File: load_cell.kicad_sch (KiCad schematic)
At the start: 10 parts, among them Q2 S8550, U7 HX711

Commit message: Remove duplicated power flag.
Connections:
- net +3.3V renamed +3V3
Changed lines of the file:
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@@
+	)
+	(symbol
+		(lib_id "power:+3V3")
+		(at 154.94 69.85 0)
+		(unit 1)
+		(body_style 1)
+		(exclude_from_sim no)
+		(in_bom yes)
+		(on_board yes)
+		(in_pos_files yes)
+		(dnp no)
+		(fields_autoplaced yes)
+		(property "Reference" "#PWR045"
+			(at 154.94 73.66 0)
+			(hide yes)
+			(show_name no)
+			(do_not_autoplace no)
+			(effects
+				(font
+					(size 1.27 1.27)
+				)
+			)
+		)
+		(property "Value" "+3V3"
+			(at 154.94 64.77 0)
+			(show_name no)
+			(do_not_autoplace no)
+			(effects
+				(font
+					(size 1.27 1.27)
+				)
+			)
+		)
+		(property "Footprint" ""
+			(at 154.94 69.85 0)
+			(hide yes)
+			(show_name no)
+			(do_not_autoplace no)
+			(effects
+				(font
+					(size 1.27 1.27)
+				)
+			)
+		)
+		(property "Datasheet" ""
+			(at 154.94 69.85 0)
+			(hide yes)
+			(show_name no)
+			(do_not_autoplace no)
+			(effects
+				(font
+					(size 1.27 1.27)
+				)
+			)
+		)
+		(property "Description" "Power symbol creates a global label with name \"+3V3\""
+			(at 154.94 69.85 0)
+			(hide yes)
+			(show_name no)
+			(do_not_autoplace no)
+			(effects
+				(font
+					(size 1.27 1.27)
+				)
+			)
+		)
+		(pin "1"
+		)
+		(instances
+			(project "CC3501-project-hardware"
+				(path "/4a2d49bb-8ba4-4c60-a8f0-05b8d2544445/0c27bcac-fbf5-401f-bcb4-99ca27aa5914"
+					(reference "#PWR045")
+					(unit 1)
+				)
+			)
+		)
 	)
 	(symbol
@@
 					(unit 1)
 				)
-			)
-		)
-	)
-	(symbol
-		(lib_id "power:+3.3V")
-		(at 154.94 69.85 270)
-		(unit 1)
-		(body_style 1)
-		(exclude_from_sim no)
-		(in_bom yes)
-		(on_board yes)
-		(in_pos_files yes)
-		(dnp no)
-		(fields_autoplaced yes)
-		(property "Reference" "#PWR045"
-			(at 151.13 69.85 0)
-			(hide yes)
-			(show_name no)
-			(do_not_autoplace no)
-			(effects
-				(font
-					(size 1.27 1.27)
-				)
-			)
-		)
-		(property "Value" "+3.3V"
-			(at 158.75 69.8499 90)
-			(show_name no)
-			(do_not_autoplace no)
-			(effects
-				(font
-					(size 1.27 1.27)
-				)
-				(justify left)
-			)
-		)
-		(property "Footprint" ""
-			(at 154.94 69.85 0)
-			(hide yes)
-			(show_name no)
-			(do_not_autoplace no)
-			(effects
-				(font
-					(size 1.27 1.27)
-				)
-			)
-		)
-		(property "Datasheet" ""
-			(at 154.94 69.85 0)
-			(hide yes)
-			(show_name no)
-			(do_not_autoplace no)
-			(effects
-				(font
-					(size 1.27 1.27)
-				)
-			)
-		)
-		(property "Description" "Power symbol creates a global label with name \"+3.3V\""
-			(at 154.94 69.85 0)
-			(hide yes)
-			(show_name no)
-			(do_not_autoplace no)
-			(effects
-				(font
-					(size 1.27 1.27)
-				)
-			)
-		)
-		(pin "1"
-		)
-		(instances
-			(project "CC3501-project-hardware"
-				(path "/4a2d49bb-8ba4-4c60-a8f0-05b8d2544445/0c27bcac-fbf5-401f-bcb4-99ca27aa5914"
-					(reference "#PWR045")
-					(unit 1)
-				)

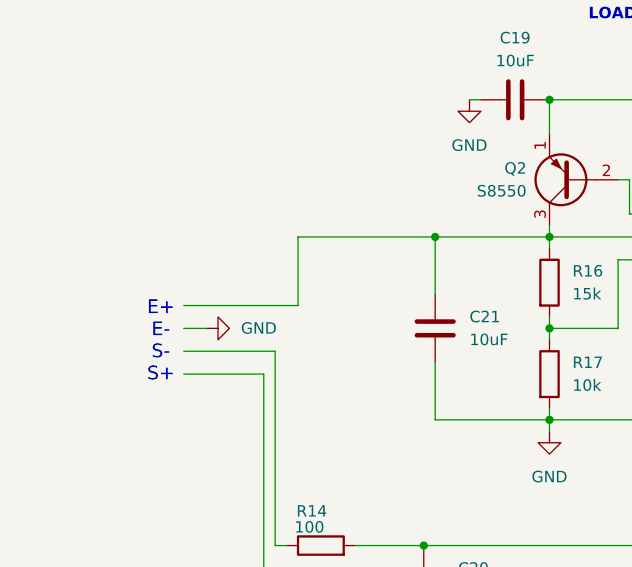
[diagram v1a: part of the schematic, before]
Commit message: Rewire TFT display to power with 5V and allowing backlight switching via FET.
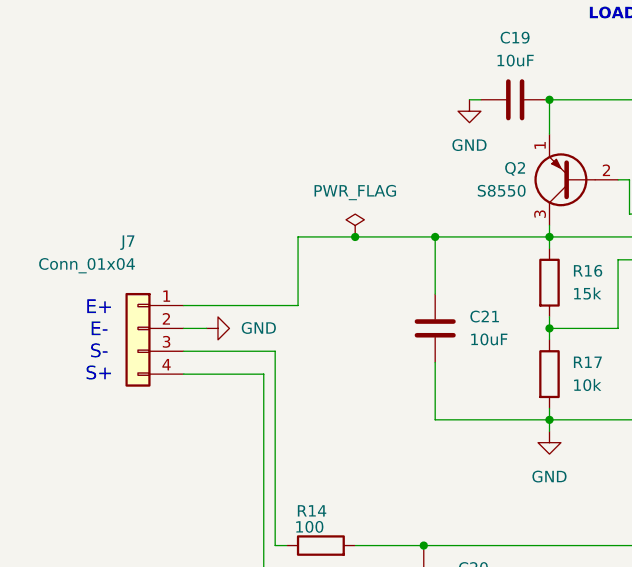
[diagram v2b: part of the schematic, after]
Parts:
- added J7: Conn_01x04, symbol Connector_Generic:Conn_01x04
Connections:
- net GND: now also J7.2 (Pin_2)
- net at R15.2: now also J7.4 (Pin_4)
- net at C21.1, Q2.3 (C), R16.1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: now also J7.1 (Pin_1)
- net at R14.1: now also J7.3 (Pin_3)
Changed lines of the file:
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@@
 	(text "E+\nE-\nS-\nS+\n"
 		(exclude_from_sim no)
-		(at 59.69 96.774 0)
+		(at 52.832 96.774 0)
 		(effects
 			(font
@@
 		(color 0 0 0 0)
 	)
+	(junction
+		(at 81.28 85.09)
+		(diameter 0)
+		(color 0 0 0 0)
+	)
 	(no_connect
 		(at 167.64 95.25)
@@
 	(wire
 		(pts
+			(xy 81.28 85.09) (xy 90.17 85.09)
+		)
+		(stroke
+			(width 0)
+			(type default)
+		)
+	)
+	(wire
+		(pts
 			(xy 138.43 115.57) (xy 138.43 116.84)
 		)
@@
 	(wire
 		(pts
-			(xy 74.93 85.09) (xy 90.17 85.09)
+			(xy 74.93 85.09) (xy 81.28 85.09)
 		)
 		(stroke
@@
 	)
 	(symbol
+		(lib_id "power:PWR_FLAG")
+		(at 81.28 85.09 0)
+		(unit 1)
+		(body_style 1)
+		(exclude_from_sim no)
+		(in_bom yes)
+		(on_board yes)
+		(in_pos_files yes)
+		(dnp no)
+		(fields_autoplaced yes)
+		(property "Reference" "#FLG06"
+			(at 81.28 83.185 0)
+			(hide yes)
+			(show_name no)
+			(do_not_autoplace no)
+			(effects
+				(font
+					(size 1.27 1.27)
+				)
+			)
+		)
+		(property "Value" "PWR_FLAG"
+			(at 81.28 80.01 0)
+			(show_name no)
+			(do_not_autoplace no)
+			(effects
+				(font
+					(size 1.27 1.27)
+				)
+			)
+		)
+		(property "Footprint" ""
+			(at 81.28 85.09 0)
+			(hide yes)
+			(show_name no)
+			(do_not_autoplace no)
+			(effects
+				(font
+					(size 1.27 1.27)
+				)
+			)
+		)
+		(property "Datasheet" ""
+			(at 81.28 85.09 0)
+			(hide yes)
+			(show_name no)
+			(do_not_autoplace no)
+			(effects
+				(font
+					(size 1.27 1.27)
+				)
+			)
+		)
+		(property "Description" "Special symbol for telling ERC where power comes from"
+			(at 81.28 85.09 0)
+			(hide yes)
+			(show_name no)
+			(do_not_autoplace no)
+			(effects
+				(font
+					(size 1.27 1.27)
+				)
+			)
+		)
+		(pin "1"
+		)
+		(instances
+			(project "CC3501-project-hardware"
+				(path "/4a2d49bb-8ba4-4c60-a8f0-05b8d2544445/0c27bcac-fbf5-401f-bcb4-99ca27aa5914"
+					(reference "#FLG06")
+					(unit 1)
+				)
+			)
+		)
+	)
+	(symbol
 		(lib_id "power:GND")
 		(at 102.87 106.68 0)
@@
 					(unit 1)
 				)
+			)
+		)
+	)
+	(symbol
+		(lib_id "Connector_Generic:Conn_01x04")
+		(at 57.15 95.25 0)
+		(mirror y)
+		(unit 1)
+		(body_style 1)
+		(exclude_from_sim no)
+		(in_bom yes)
+		(on_board yes)
+		(in_pos_files yes)
+		(dnp no)
+		(property "Reference" "J7"
+			(at 56.896 85.598 0)
+			(show_name no)
+			(do_not_autoplace no)
+			(effects
+				(font
+					(size 1.27 1.27)
+				)
+				(justify left)
+			)
+		)
+		(property "Value" "Conn_01x04"
+			(at 56.896 88.138 0)
+			(show_name no)
+			(do_not_autoplace no)
+			(effects
+				(font
+					(size 1.27 1.27)
+				)
+				(justify left)
+			)
+		)
+		(property "Footprint" ""
+			(at 57.15 95.25 0)
+			(hide yes)
+			(show_name no)
+			(do_not_autoplace no)
+			(effects
+				(font
+					(size 1.27 1.27)
+				)
+			)
+		)
+		(property "Datasheet" ""
+			(at 57.15 95.25 0)
+			(hide yes)
+			(show_name no)
+			(do_not_autoplace no)
+			(effects
+				(font
+					(size 1.27 1.27)
+				)
+			)
+		)
+		(property "Description" "Generic connector, single row, 01x04, script generated (kicad-library-utils/schlib/autogen/connector/)"
+			(at 57.15 95.25 0)
+			(hide yes)
+			(show_name no)
+			(do_not_autoplace no)
+			(effects
+				(font
+					(size 1.27 1.27)
+				)
+			)
+		)
+		(pin "2"
+		)
+		(pin "1"
+		)
+		(pin "4"
+		)
+		(pin "3"
+		)
+		(instances
+			(project "CC3501-project-hardware"
+				(path "/4a2d49bb-8ba4-4c60-a8f0-05b8d2544445/0c27bcac-fbf5-401f-bcb4-99ca27aa5914"
+					(reference "J7")
+					(unit 1)
+				)

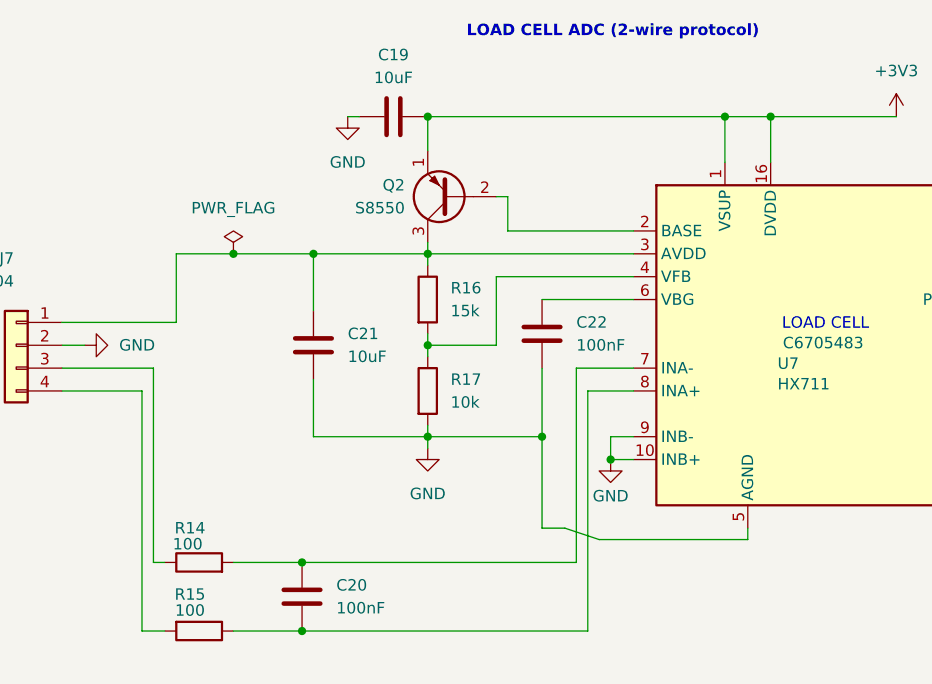
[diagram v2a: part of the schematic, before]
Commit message: edit HX711 config
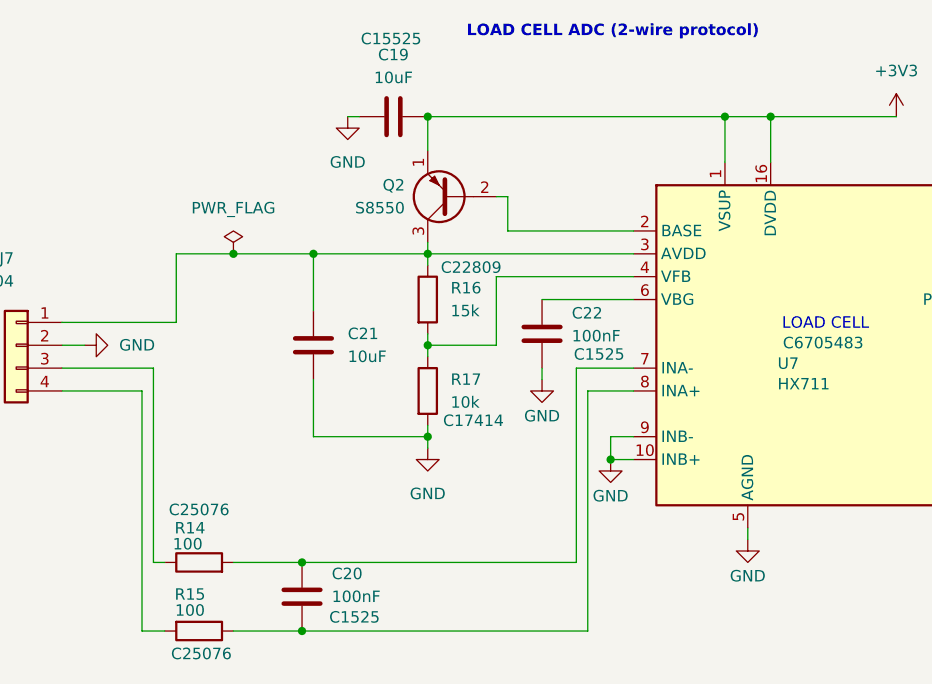
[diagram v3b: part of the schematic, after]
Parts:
- J7: footprint (none) -> Connector_PinHeader_2.54mm:PinHeader_1x04_P2.54mm_Vertical
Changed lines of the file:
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@@
 	)
 	(junction
-		(at 115.57 105.41)
-		(diameter 0)
-		(color 0 0 0 0)
-	)
-	(junction
 		(at 102.87 69.85)
 		(diameter 0)
@@
 	(wire
 		(pts
-			(xy 121.92 116.84) (xy 138.43 116.84)
-		)
-		(stroke
-			(width 0)
-			(type default)
-		)
-	)
-	(wire
-		(pts
 			(xy 72.39 119.38) (xy 73.66 119.38)
 		)
@@
 	(wire
 		(pts
-			(xy 115.57 97.79) (xy 115.57 105.41)
-		)
-		(stroke
-			(width 0)
-			(type default)
-		)
-	)
-	(wire
-		(pts
 			(xy 102.87 85.09) (xy 125.73 85.09)
 		)
@@
 	(wire
 		(pts
-			(xy 115.57 115.57) (xy 118.11 115.57)
-		)
-		(stroke
-			(width 0)
-			(type default)
-		)
-	)
-	(wire
-		(pts
 			(xy 140.97 69.85) (xy 140.97 74.93)
 		)
@@
 	(wire
 		(pts
-			(xy 118.11 115.57) (xy 121.92 116.84)
-		)
-		(stroke
-			(width 0)
-			(type default)
-		)
-	)
-	(wire
-		(pts
 			(xy 110.49 78.74) (xy 111.76 78.74)
 		)
@@
 	(wire
 		(pts
+			(xy 115.57 97.79) (xy 115.57 99.06)
+		)
+		(stroke
+			(width 0)
+			(type default)
+		)
+	)
+	(wire
+		(pts
 			(xy 102.87 104.14) (xy 102.87 105.41)
 		)
@@
 	(wire
 		(pts
-			(xy 102.87 105.41) (xy 115.57 105.41)
-		)
-		(stroke
-			(width 0)
-			(type default)
-		)
-	)
-	(wire
-		(pts
 			(xy 102.87 105.41) (xy 90.17 105.41)
 		)
@@
 	(wire
 		(pts
-			(xy 115.57 105.41) (xy 115.57 115.57)
-		)
-		(stroke
-			(width 0)
-			(type default)
-		)
-	)
-	(wire
-		(pts
 			(xy 120.65 100.33) (xy 120.65 127)
 		)
@@
 	(symbol
 		(lib_id "power:GND")
+		(at 115.57 99.06 0)
+		(unit 1)
+		(body_style 1)
+		(exclude_from_sim no)
+		(in_bom yes)
+		(on_board yes)
+		(in_pos_files yes)
+		(dnp no)
+		(property "Reference" "#PWR082"
+			(at 115.57 105.41 0)
+			(hide yes)
+			(show_name no)
+			(do_not_autoplace no)
+			(effects
+				(font
+					(size 1.27 1.27)
+				)
+			)
+		)
+		(property "Value" "GND"
+			(at 115.57 103.124 0)
+			(show_name no)
+			(do_not_autoplace no)
+			(effects
+				(font
+					(size 1.27 1.27)
+				)
+			)
+		)
+		(property "Footprint" ""
+			(at 115.57 99.06 0)
+			(hide yes)
+			(show_name no)
+			(do_not_autoplace no)
+			(effects
+				(font
+					(size 1.27 1.27)
+				)
+			)
+		)
+		(property "Datasheet" ""
+			(at 115.57 99.06 0)
+			(hide yes)
+			(show_name no)
+			(do_not_autoplace no)
+			(effects
+				(font
+					(size 1.27 1.27)
+				)
+			)
+		)
+		(property "Description" "Power symbol creates a global label with name \"GND\" , ground"
+			(at 115.57 99.06 0)
+			(hide yes)
+			(show_name no)
+			(do_not_autoplace no)
+			(effects
+				(font
+					(size 1.27 1.27)
+				)
+			)
+		)
+		(pin "1"
+		)
+		(instances
+			(project "CC3501-project-hardware"
+				(path "/4a2d49bb-8ba4-4c60-a8f0-05b8d2544445/0c27bcac-fbf5-401f-bcb4-99ca27aa5914"
+					(reference "#PWR082")
+					(unit 1)
+				)
+			)
+		)
+	)
+	(symbol
+		(lib_id "power:GND")
 		(at 102.87 106.68 0)
 		(unit 1)
@@
 		)
 		(property "LCSC PN" "C25076"
-			(at 77.47 127 90)
-			(hide yes)
+			(at 77.724 129.54 90)
 			(show_name no)
 			(do_not_autoplace no)
@@
 		)
 		(property "LCSC PN" "C15525"
-			(at 99.06 69.85 90)
-			(hide yes)
+			(at 98.806 61.214 90)
 			(show_name no)
 			(do_not_autoplace no)
@@
 		(in_pos_files yes)
 		(dnp no)
-		(fields_autoplaced yes)
 		(property "Reference" "R17"
 			(at 105.41 99.0599 0)
@@
 		)
 		(property "LCSC PN" "C17414"
-			(at 102.87 100.33 0)
-			(hide yes)
+			(at 107.95 103.632 0)
 			(show_name no)
 			(do_not_autoplace no)
@@
 		(in_pos_files yes)
 		(dnp no)
-		(fields_autoplaced yes)
 		(property "Reference" "R16"
 			(at 105.41 88.8999 0)
@@
 		)
 		(property "LCSC PN" "C22809"
-			(at 102.87 90.17 0)
-			(hide yes)
+			(at 107.696 86.614 0)
 			(show_name no)
 			(do_not_autoplace no)
@@
 		)
 		(property "LCSC PN" "C25076"
-			(at 77.47 119.38 90)
-			(hide yes)
+			(at 77.47 113.538 90)
 			(show_name no)
 			(do_not_autoplace no)
@@
 		(in_pos_files yes)
 		(dnp no)
-		(fields_autoplaced yes)
 		(property "Reference" "C22"
-			(at 119.38 92.7099 0)
+			(at 118.872 91.694 0)
 			(show_name no)
 			(do_not_autoplace no)
@@
 		)
 		(property "Value" "100nF"
-			(at 119.38 95.2499 0)
+			(at 118.872 94.234 0)
 			(show_name no)
 			(do_not_autoplace no)
@@
 		)
 		(property "LCSC PN" "C1525"
-			(at 115.57 93.98 0)
-			(hide yes)
+			(at 121.92 96.2661 0)
 			(show_name no)
 			(do_not_autoplace no)
@@
 		(in_pos_files yes)
 		(dnp no)
-		(fields_autoplaced yes)
 		(property "Reference" "C20"
-			(at 92.71 121.9199 0)
+			(at 92.202 120.65 0)
 			(show_name no)
 			(do_not_autoplace no)
@@
 		)
 		(property "Value" "100nF"
-			(at 92.71 124.4599 0)
+			(at 92.202 123.19 0)
 			(show_name no)
 			(do_not_autoplace no)
@@
 		)
 		(property "LCSC PN" "C1525"
-			(at 88.9 123.19 0)
-			(hide yes)
+			(at 94.742 125.476 0)
 			(show_name no)
 			(do_not_autoplace no)
@@
 			)
 		)
-		(property "Footprint" ""
+		(property "Footprint" "Connector_PinHeader_2.54mm:PinHeader_1x04_P2.54mm_Vertical"
 			(at 57.15 95.25 0)
 			(hide yes)
@@
 					(unit 1)
 				)
+			)
+		)
+	)
+	(symbol
+		(lib_id "power:GND")
+		(at 138.43 116.84 0)
+		(unit 1)
+		(body_style 1)
+		(exclude_from_sim no)
+		(in_bom yes)
+		(on_board yes)
+		(in_pos_files yes)
+		(dnp no)
+		(property "Reference" "#PWR043"
+			(at 138.43 123.19 0)
+			(hide yes)
+			(show_name no)
+			(do_not_autoplace no)
+			(effects
+				(font
+					(size 1.27 1.27)
+				)
+			)
+		)
+		(property "Value" "GND"
+			(at 138.43 120.904 0)
+			(show_name no)
+			(do_not_autoplace no)
+			(effects
+				(font
+					(size 1.27 1.27)
+				)
+			)
+		)
+		(property "Footprint" ""
+			(at 138.43 116.84 0)
+			(hide yes)
+			(show_name no)
+			(do_not_autoplace no)
+			(effects
+				(font
+					(size 1.27 1.27)
+				)
+			)
+		)
+		(property "Datasheet" ""
+			(at 138.43 116.84 0)
+			(hide yes)
+			(show_name no)
+			(do_not_autoplace no)
+			(effects
+				(font
+					(size 1.27 1.27)
+				)
+			)
+		)
+		(property "Description" "Power symbol creates a global label with name \"GND\" , ground"
+			(at 138.43 116.84 0)
+			(hide yes)
+			(show_name no)
+			(do_not_autoplace no)
+			(effects
+				(font
+					(size 1.27 1.27)
+				)
+			)
+		)
+		(pin "1"
+		)
+		(instances
+			(project "CC3501-project-hardware"
+				(path "/4a2d49bb-8ba4-4c60-a8f0-05b8d2544445/0c27bcac-fbf5-401f-bcb4-99ca27aa5914"
+					(reference "#PWR043")
+					(unit 1)
+				)

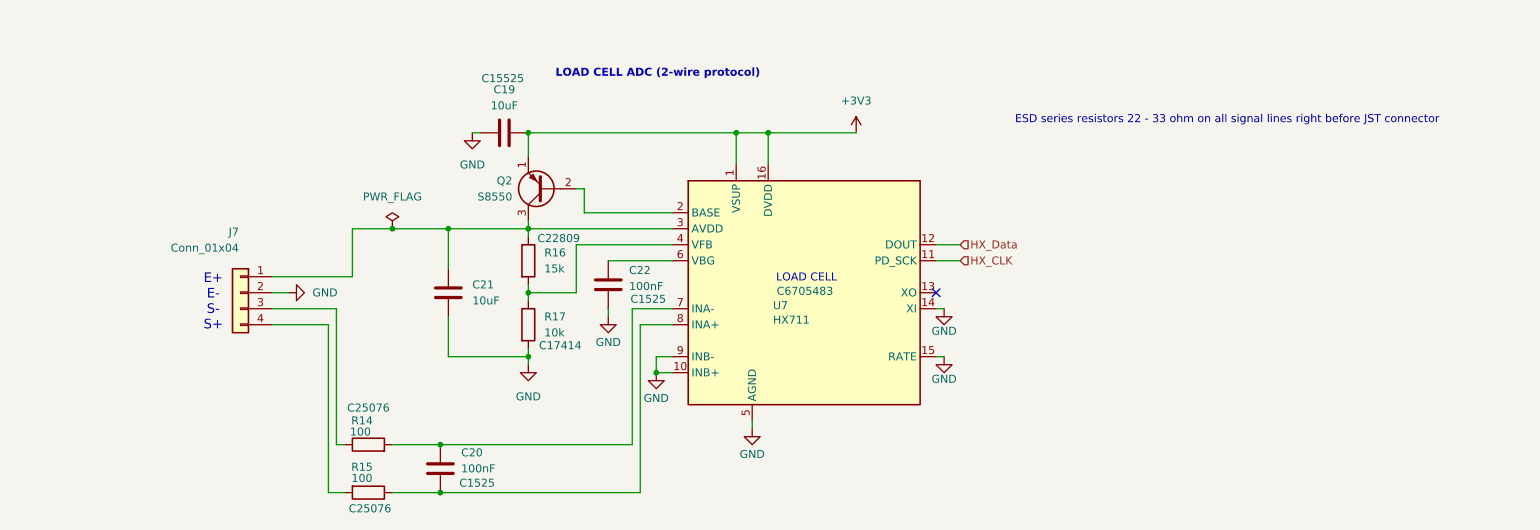
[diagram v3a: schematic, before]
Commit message: edit HX711 configuration to match datasheet and sparkfun example as well as add JLC part numbers and display them on schematic
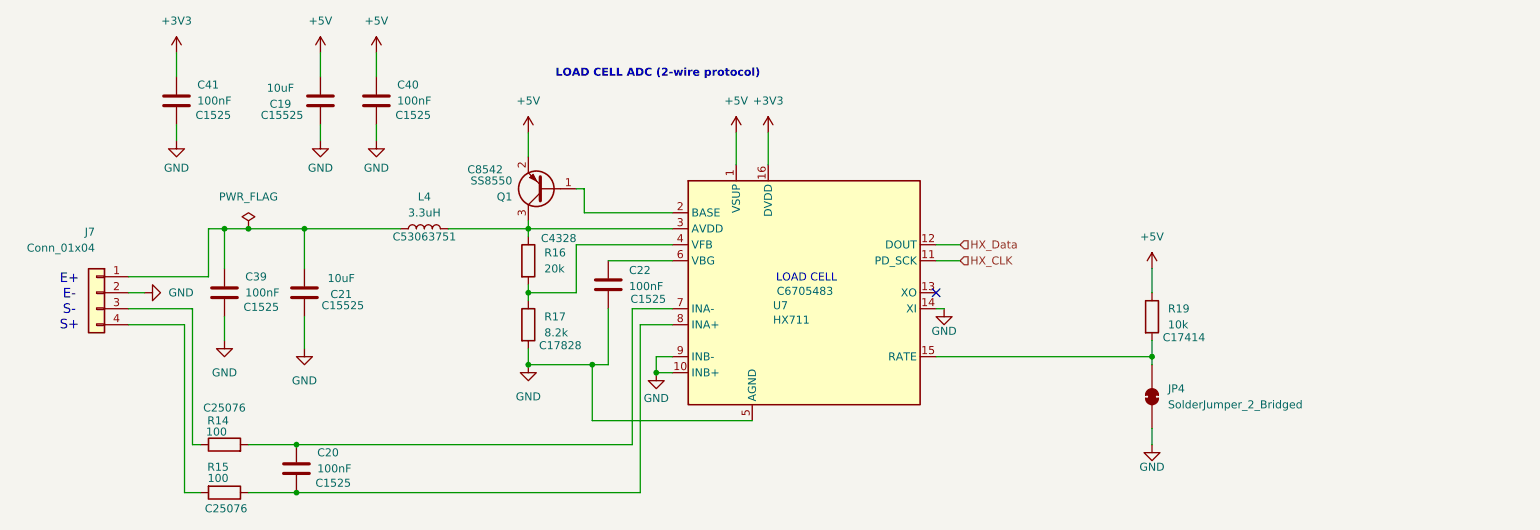
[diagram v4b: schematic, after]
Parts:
- removed Q2: S8550, Package_TO_SOT_THT:TO-92_Inline, symbol Transistor_BJT:S8550
- added C39, C40, C41: 100nF, Capacitor_SMD:C_0402_1005Metric, symbol Device:C
- added JP4: SolderJumper_2_Bridged, Jumper:SolderJumper-2_P1.3mm_Bridged2Bar_RoundedPad1.0x1.5mm, symbol Jumper:SolderJumper_2_Bridged
- added L4: 3.3uH, Inductor_SMD:L_0805_2012Metric, symbol Device:L
- added Q1: SS8550, Package_TO_SOT_SMD:SOT-23, symbol Transistor_BJT:SS8550
- added R19: 10k, Resistor_SMD:R_0805_2012Metric, symbol Device:R
- R16: value 15k -> 20k; footprint Resistor_SMD:R_0603_1608Metric -> Resistor_SMD:R_0805_2012Metric; LCSC PN C22809 -> C4328
- R17: value 10k -> 8.2k; LCSC PN C17414 -> C17828
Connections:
- net +3V3: now also C41.1; no longer C19.2, U7.1 (VSUP)
- net GND: now also C21.1, C39.2, C40.2, C41.2, JP4.1 (A); no longer C21.2, U7.15 (RATE)
- net at U7.2 (BASE): now also Q1.1 (B)
- net at R16.1, U7.3 (AVDD): now also L4.2, Q1.3 (C); no longer C21.1, J7.1 (Pin_1)
- new net: JP4.2 (B), R19.2, U7.15 (RATE)
- new net: C21.2, C39.1, J7.1 (Pin_1), L4.1
- new net +5V: C19.2, C40.1, Q1.2 (E), R19.1, U7.1 (VSUP)
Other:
- note removed: "ESD series resistors 22 - 33 ohm on all signal lines right before JST connector"
- moved on the sheet: C19, C20, J7, R14, R15
